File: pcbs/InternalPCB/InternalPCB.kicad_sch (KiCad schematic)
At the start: 16 parts, among them J1 Conn_01x20, J10 694106301002, J2 Conn_01x20, J3 Conn_01x04_Pin, J4 Conn_01x04_Pin, J5 Conn_01x02_Pin, J6 Conn_01x04_Pin, J7 Conn_01x03_Pin, J8 Conn_01x05_Pin, J9 Conn_01x05_Pin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

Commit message: 3,3V für RTC ausgeführt
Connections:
- net 3.3V: now also J1.5 (Pin_5), U1.36 (3V3)
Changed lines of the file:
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@@
+    )
+  )
+  (global_label "3.3V" (shape output) (at 106.68 49.53 0) (fields_autoplaced)
+    (effects (font (size 1.27 1.27)) (justify left))
+    (property "Intersheetrefs" "${INTERSHEET_REFS}" (at 113.7776 49.53 0)
+      (effects (font (size 1.27 1.27)) (justify left) hide)
     )
   )
@@
     )
   )
+  (global_label "3.3V" (shape output) (at 107.95 125.73 0) (fields_autoplaced)
+    (effects (font (size 1.27 1.27)) (justify left))
+    (property "Intersheetrefs" "${INTERSHEET_REFS}" (at 115.0476 125.73 0)
+      (effects (font (size 1.27 1.27)) (justify left) hide)
+    )
+  )

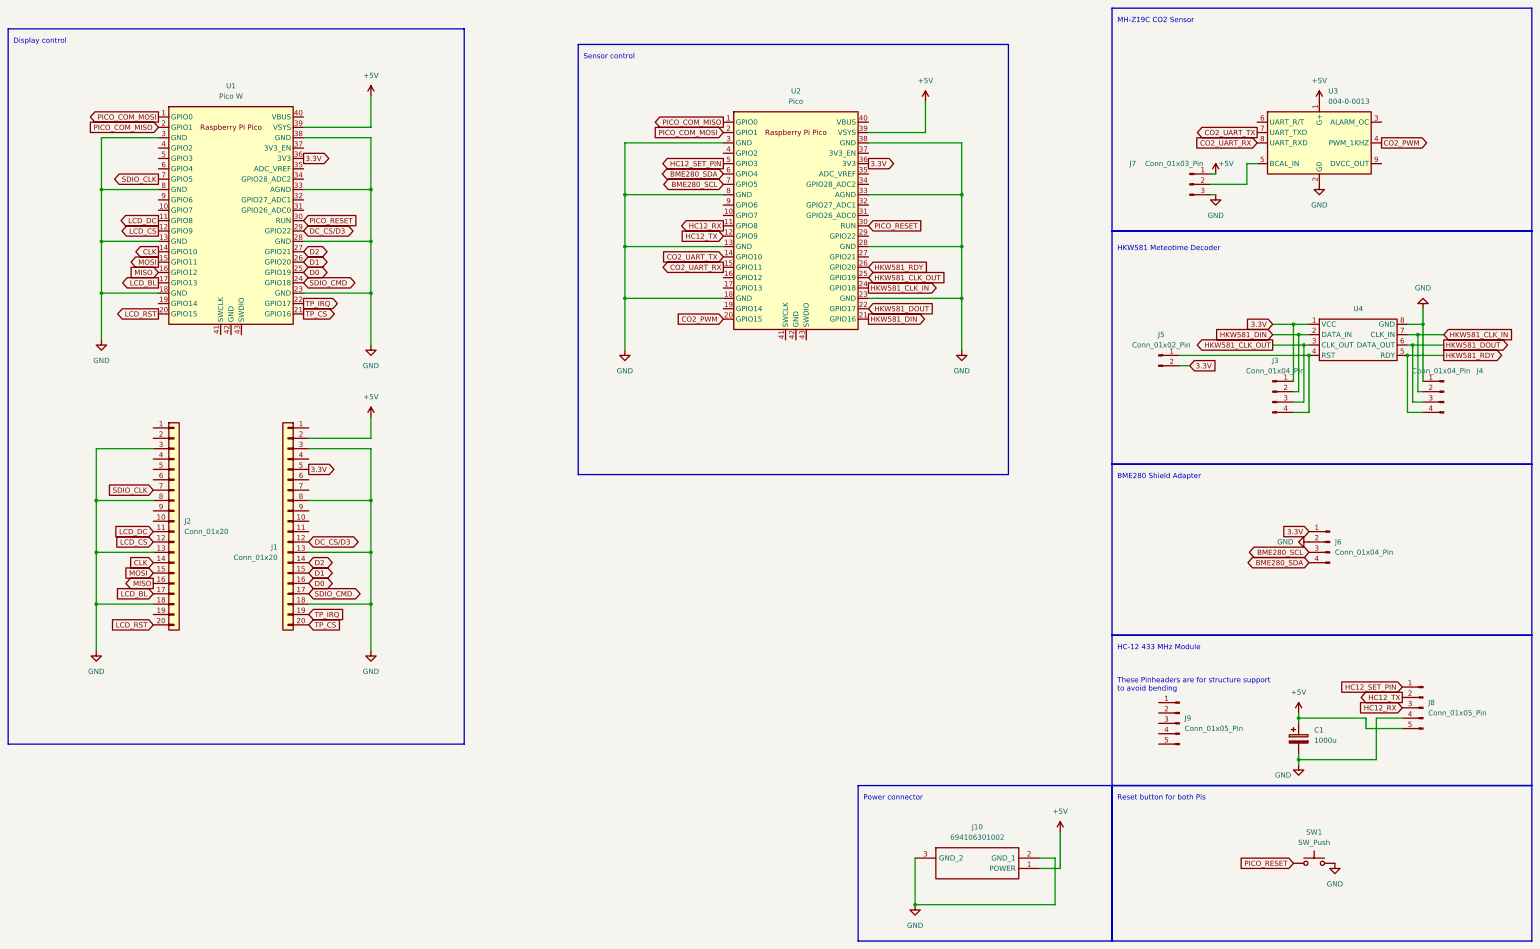
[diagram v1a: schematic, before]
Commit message: PCB Innenmodul verbessert
- Löcher für Displaymontage
- 2. Stromanschluss für Wandmontage
- M3 Löcher für Gehäuse und Wandmontage
- Beschriftung angepasst
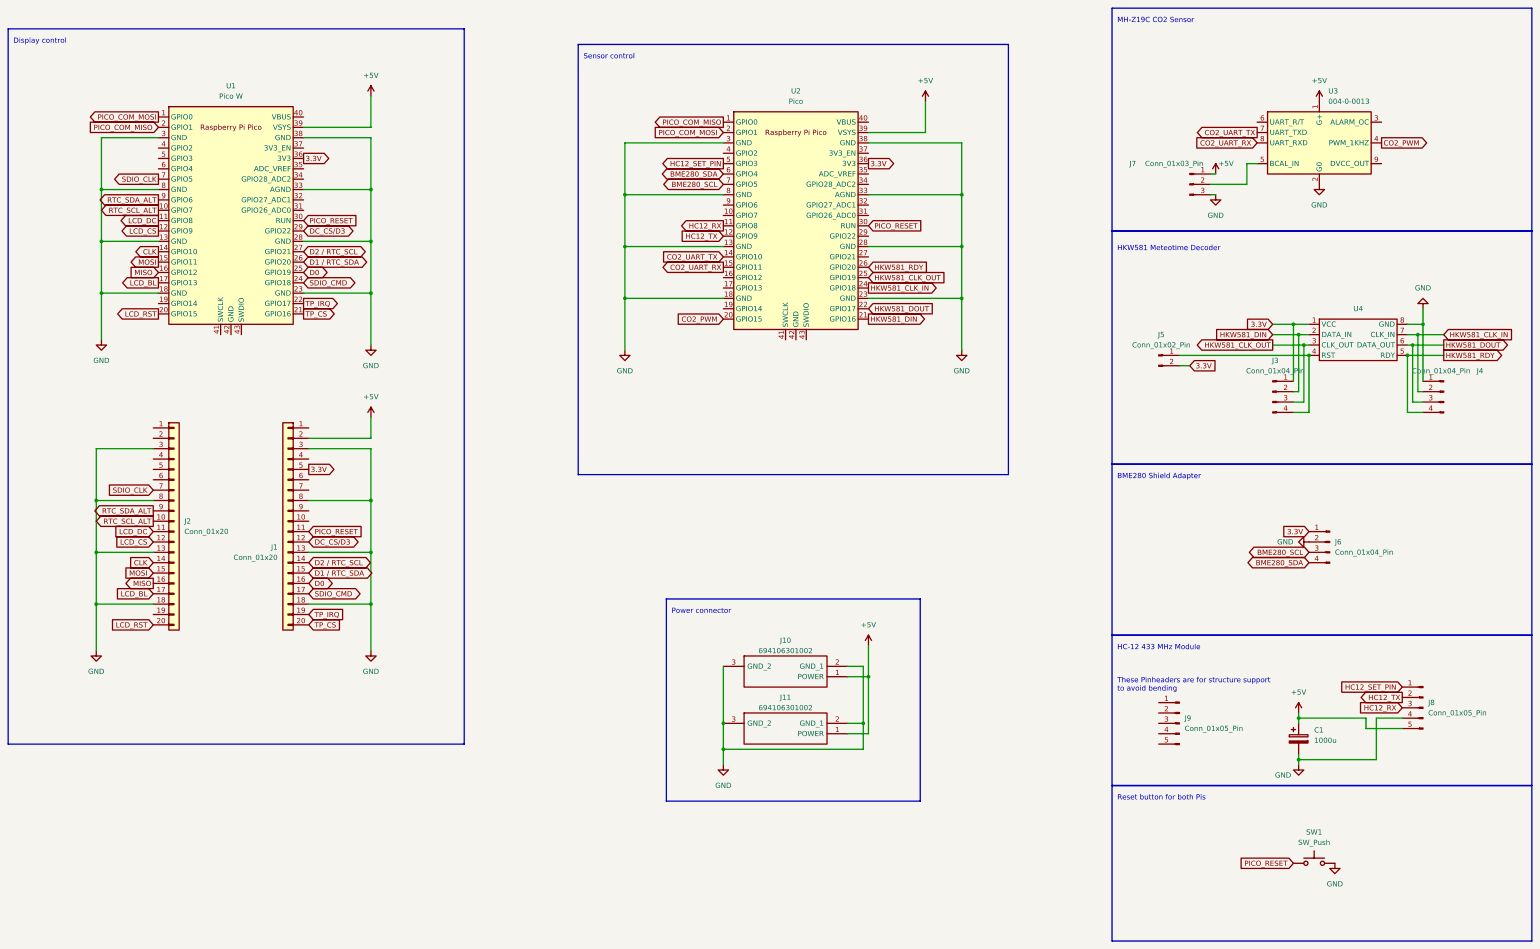
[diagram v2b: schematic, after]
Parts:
- added J11: 694106301002, 694106301002:694106301002_1, symbol 694106301002:694106301002
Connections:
- net +5V: now also J11.1 (POWER)
- net GND: now also J11.2 (GND_1), J11.3 (GND_2)
- net PICO_RESET: now also J1.11 (Pin_11)
- net RTC_SCL_ALT: now reaches J2.10 (Pin_10)
- net RTC_SCL_ALT: now also U1.10 (GPIO7)
- net RTC_SDA_ALT: now reaches J2.9 (Pin_9)
- net RTC_SDA_ALT: now also U1.9 (GPIO6)
- net D1 renamed D1 / RTC_SDA
- net D2 renamed D2 / RTC_SCL
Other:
- moved on the sheet: J10

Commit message: Bisschen DRC dies das
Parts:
- C1: footprint Capacitor_THT:CP_Axial_L46.0mm_D20.0mm_P52.00mm_Horizontal -> Capacitor_THT:C_Radial_D10.0mm_H16.0mm_P5.00mm
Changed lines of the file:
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@@
       (effects (font (size 1.27 1.27)) (justify left))
     )
-    (property "Footprint" "Capacitor_THT:CP_Axial_L46.0mm_D20.0mm_P52.00mm_Horizontal" (at 351.4852 195.58 0)
-      (effects (font (size 1.27 1.27)) hide)
+    (property "Footprint" "Capacitor_THT:C_Radial_D10.0mm_H16.0mm_P5.00mm" (at 351.4852 195.58 0)
+      (effects (font (size 1.27 1.27)))
     )
     (property "Datasheet" "~" (at 350.52 191.77 0)
